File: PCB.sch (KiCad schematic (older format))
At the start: 30 parts

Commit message: Change mounting holes to slots to suit multiple box vendors with variable mounting positions. - Move GPIO Connect along and re-routed. (removed 'edge' trace) - Move VIN_Prot to near main power connector - Moved I2C Headers to board edge, and 1-wire inboard. I2C Can now be more easily used by HAT's - Moved Blue Led next to RED Led, and labeled - Updated both silkscreens accordingly
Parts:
- H1001, H1002: footprint SH-ESP32:MountingHole_3.2mm_M3_Unplated -> SH-ESP32:MountingSlot_3.2mm_M3_Unplated
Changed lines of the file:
@@
 F 0 "H1001" H 2000 1896 50  0000 L CNN
 F 1 "MountingHole" H 2000 1805 50  0000 L CNN
-F 2 "SH-ESP32:MountingHole_3.2mm_M3_Unplated" H 1900 1850 50  0001 C CNN
+F 2 "SH-ESP32:MountingSlot_3.2mm_M3_Unplated" H 1900 1850 50  0001 C CNN
 F 3 "~" H 1900 1850 50  0001 C CNN
 	1    1900 1850
@@
 F 0 "H1002" H 2000 2196 50  0000 L CNN
 F 1 "MountingHole" H 2000 2105 50  0000 L CNN
-F 2 "SH-ESP32:MountingHole_3.2mm_M3_Unplated" H 1900 2150 50  0001 C CNN
+F 2 "SH-ESP32:MountingSlot_3.2mm_M3_Unplated" H 1900 2150 50  0001 C CNN
 F 3 "~" H 1900 2150 50  0001 C CNN
 	1    1900 2150

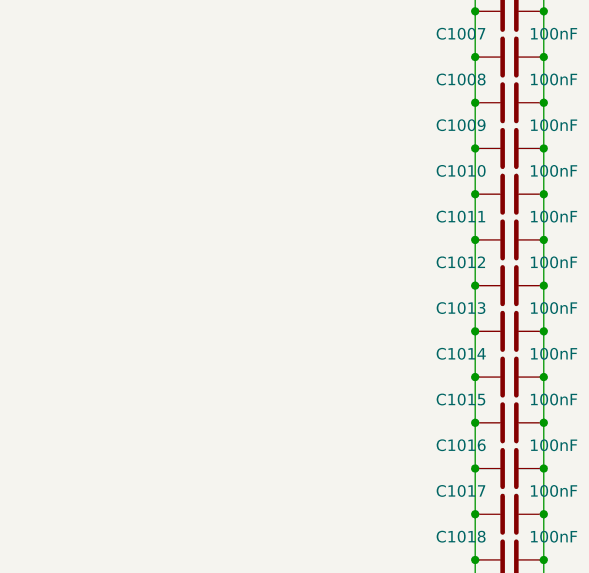
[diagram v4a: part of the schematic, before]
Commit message: Add JLCPCB tooling holes
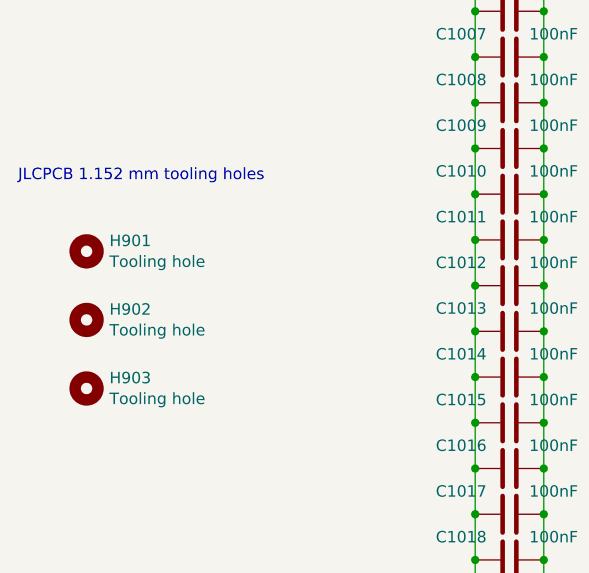
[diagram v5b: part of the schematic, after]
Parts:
- added H901, H902, H903: Tooling hole, SH-ESP32:JlcpcbToolingHole, symbol Mechanical:MountingHole
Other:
- note added: "JLCPCB 1.152 mm tooling holes"
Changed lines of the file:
@@
 	4700 3250 4700 3050
 Connection ~ 4400 3250
+$Comp
+L Mechanical:MountingHole H901
+U 1 1 60160A7D
+P 1900 3900
+F 0 "H901" H 2000 3946 50  0000 L CNN
+F 1 "Tooling hole" H 2000 3855 50  0000 L CNN
+F 2 "SH-ESP32:JlcpcbToolingHole" H 1900 3900 50  0001 C CNN
+F 3 "~" H 1900 3900 50  0001 C CNN
+	1    1900 3900
+	1    0    0    -1
+$EndComp
+$Comp
+L Mechanical:MountingHole H902
+U 1 1 601616D4
+P 1900 4200
+F 0 "H902" H 2000 4246 50  0000 L CNN
+F 1 "Tooling hole" H 2000 4155 50  0000 L CNN
+F 2 "SH-ESP32:JlcpcbToolingHole" H 1900 4200 50  0001 C CNN
+F 3 "~" H 1900 4200 50  0001 C CNN
+	1    1900 4200
+	1    0    0    -1
+$EndComp
+$Comp
+L Mechanical:MountingHole H903
+U 1 1 6016213C
+P 1900 4500
+F 0 "H903" H 2000 4546 50  0000 L CNN
+F 1 "Tooling hole" H 2000 4455 50  0000 L CNN
+F 2 "SH-ESP32:JlcpcbToolingHole" H 1900 4500 50  0001 C CNN
+F 3 "~" H 1900 4500 50  0001 C CNN
+	1    1900 4500
+	1    0    0    -1
+$EndComp
+Text Notes 1600 3600 0    50   ~ 0
+JLCPCB 1.152 mm tooling holes
 $EndSCHEMATC
